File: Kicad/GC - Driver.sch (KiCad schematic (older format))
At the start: 45 parts, among them U3 DRV8302

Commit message: Passives changed from 0805 to 0603
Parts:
- C21, C22, C23, C24, C25, C26, C27, C28, C32, C33, C34, C35, C36, C37: footprint Capacitors_SMD:C_0805 -> Capacitors_SMD:C_0603
- R26, R27, R28, R29, R30, R31, R32, R33, R34, R35, R36, R39, R40, R41, R42, R43: footprint Resistors_SMD:R_0805 -> Resistors_SMD:R_0603
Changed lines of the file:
@@
 F 0 "R36" V 10100 3350 50  0000 C CNN
 F 1 "39k" V 10200 3350 50  0000 C CNN
-F 2 "Resistors_SMD:R_0805" H 10200 3350 60  0001 C CNN
+F 2 "Resistors_SMD:R_0603" H 10200 3350 60  0001 C CNN
 F 3 "" H 10200 3350 60  0001 C CNN
 	1    10200 3350
@@
 F 0 "R39" V 10300 3450 50  0000 C CNN
 F 1 "2k2" V 10200 3450 50  0000 C CNN
-F 2 "Resistors_SMD:R_0805" H 10200 3450 60  0001 C CNN
+F 2 "Resistors_SMD:R_0603" H 10200 3450 60  0001 C CNN
 F 3 "" H 10200 3450 60  0001 C CNN
 	1    10200 3450
@@
 F 0 "R41" V 10300 3950 50  0000 C CNN
 F 1 "2k2" V 10200 3950 50  0000 C CNN
-F 2 "Resistors_SMD:R_0805" H 10200 3950 60  0001 C CNN
+F 2 "Resistors_SMD:R_0603" H 10200 3950 60  0001 C CNN
 F 3 "" H 10200 3950 60  0001 C CNN
 	1    10200 3950
@@
 F 0 "R40" V 10100 3850 50  0000 C CNN
 F 1 "39k" V 10200 3850 50  0000 C CNN
-F 2 "Resistors_SMD:R_0805" H 10200 3850 60  0001 C CNN
+F 2 "Resistors_SMD:R_0603" H 10200 3850 60  0001 C CNN
 F 3 "" H 10200 3850 60  0001 C CNN
 	1    10200 3850
@@
 F 0 "R42" V 10100 4300 50  0000 C CNN
 F 1 "39k" V 10200 4300 50  0000 C CNN
-F 2 "Resistors_SMD:R_0805" H 10200 4300 60  0001 C CNN
+F 2 "Resistors_SMD:R_0603" H 10200 4300 60  0001 C CNN
 F 3 "" H 10200 4300 60  0001 C CNN
 	1    10200 4300
@@
 F 0 "R43" V 10300 4400 50  0000 C CNN
 F 1 "2k2" V 10200 4400 50  0000 C CNN
-F 2 "Resistors_SMD:R_0805" H 10200 4400 60  0001 C CNN
+F 2 "Resistors_SMD:R_0603" H 10200 4400 60  0001 C CNN
 F 3 "" H 10200 4400 60  0001 C CNN
 	1    10200 4400
@@
 F 0 "C34" V 6650 3950 50  0000 L CNN
 F 1 "220nF" V 6550 3950 50  0000 L CNN
-F 2 "Capacitors_SMD:C_0805" H 6600 3850 60  0001 C CNN
+F 2 "Capacitors_SMD:C_0603" H 6600 3850 60  0001 C CNN
 F 3 "" H 6600 3850 60  0001 C CNN
 	1    6600 3850
@@
 F 0 "C35" V 6650 4450 50  0000 L CNN
 F 1 "220nF" V 6550 4450 50  0000 L CNN
-F 2 "Capacitors_SMD:C_0805" H 6600 4350 60  0001 C CNN
+F 2 "Capacitors_SMD:C_0603" H 6600 4350 60  0001 C CNN
 F 3 "" H 6600 4350 60  0001 C CNN
 	1    6600 4350
@@
 F 0 "R31" V 7300 3250 50  0000 C CNN
 F 1 "1M" V 7200 3250 50  0000 C CNN
-F 2 "Resistors_SMD:R_0805" H 7200 3250 60  0001 C CNN
+F 2 "Resistors_SMD:R_0603" H 7200 3250 60  0001 C CNN
 F 3 "" H 7200 3250 60  0001 C CNN
 	1    7200 3250
@@
 F 0 "C27" V 4300 3600 50  0000 L CNN
 F 1 "22nF" V 4300 3950 50  0000 L CNN
-F 2 "Capacitors_SMD:C_0805" H 4350 3850 60  0001 C CNN
+F 2 "Capacitors_SMD:C_0603" H 4350 3850 60  0001 C CNN
 F 3 "" H 4350 3850 60  0001 C CNN
 	1    4350 3850
@@
 F 0 "C22" V 3850 3800 50  0000 L CNN
 F 1 "2.2uF" V 3850 4150 50  0000 L CNN
-F 2 "Capacitors_SMD:C_0805" H 3900 4050 60  0001 C CNN
+F 2 "Capacitors_SMD:C_0603" H 3900 4050 60  0001 C CNN
 F 3 "" H 3900 4050 60  0001 C CNN
 	1    3900 4050
@@
 F 0 "C25" V 4050 4850 50  0000 L CNN
 F 1 "2.2uF" V 3950 4850 50  0000 L CNN
-F 2 "Capacitors_SMD:C_0805" H 4000 4750 60  0001 C CNN
+F 2 "Capacitors_SMD:C_0603" H 4000 4750 60  0001 C CNN
 F 3 "" H 4000 4750 60  0001 C CNN
 	1    4000 4750
@@
 F 0 "R28" V 3850 3150 50  0000 C CNN
 F 1 "10k" V 3950 3150 50  0000 C CNN
-F 2 "Resistors_SMD:R_0805" H 3950 3150 60  0001 C CNN
+F 2 "Resistors_SMD:R_0603" H 3950 3150 60  0001 C CNN
 F 3 "" H 3950 3150 60  0001 C CNN
 	1    3950 3150
@@
 F 0 "R30" V 4600 2300 50  0000 C CNN
 F 1 "220k" V 4500 2300 50  0000 C CNN
-F 2 "Resistors_SMD:R_0805" H 4500 2300 60  0001 C CNN
+F 2 "Resistors_SMD:R_0603" H 4500 2300 60  0001 C CNN
 F 3 "" H 4500 2300 60  0001 C CNN
 	1    4500 2300
@@
 F 0 "C26" H 4050 2200 50  0000 L CNN
 F 1 "6.8nF" H 4250 2200 50  0000 L CNN
-F 2 "Capacitors_SMD:C_0805" H 4250 2100 60  0001 C CNN
+F 2 "Capacitors_SMD:C_0603" H 4250 2100 60  0001 C CNN
 F 3 "" H 4250 2100 60  0001 C CNN
 	1    4250 2100
@@
 F 0 "R32" V 7100 4900 50  0000 C CNN
 F 1 "100R" V 7150 4700 50  0000 C CNN
-F 2 "Resistors_SMD:R_0805" H 7150 4700 60  0001 C CNN
+F 2 "Resistors_SMD:R_0603" H 7150 4700 60  0001 C CNN
 F 3 "" H 7150 4700 60  0001 C CNN
 	1    7150 4700
@@
 F 0 "R34" V 7100 5250 50  0000 C CNN
 F 1 "100R" V 7150 5050 50  0000 C CNN
-F 2 "Resistors_SMD:R_0805" H 7150 5050 60  0001 C CNN
+F 2 "Resistors_SMD:R_0603" H 7150 5050 60  0001 C CNN
 F 3 "" H 7150 5050 60  0001 C CNN
 	1    7150 5050
@@
 F 0 "R35" V 7100 5400 50  0000 C CNN
 F 1 "100R" V 7150 5200 50  0000 C CNN
-F 2 "Resistors_SMD:R_0805" H 7150 5200 60  0001 C CNN
+F 2 "Resistors_SMD:R_0603" H 7150 5200 60  0001 C CNN
 F 3 "" H 7150 5200 60  0001 C CNN
 	1    7150 5200
@@
 F 0 "C36" V 6550 4600 50  0000 L CNN
 F 1 "2.2nF" V 6650 4600 50  0000 L CNN
-F 2 "Capacitors_SMD:C_0805" H 6600 4850 60  0001 C CNN
+F 2 "Capacitors_SMD:C_0603" H 6600 4850 60  0001 C CNN
 F 3 "" H 6600 4850 60  0001 C CNN
 	1    6600 4850
@@
 F 0 "C37" V 6550 4950 50  0000 L CNN
 F 1 "2.2nF" V 6650 4950 50  0000 L CNN
-F 2 "Capacitors_SMD:C_0805" H 6600 5200 60  0001 C CNN
+F 2 "Capacitors_SMD:C_0603" H 6600 5200 60  0001 C CNN
 F 3 "" H 6600 5200 60  0001 C CNN
 	1    6600 5200
@@
 F 0 "C24" V 4050 4600 50  0000 L CNN
 F 1 "2.2uF" V 3950 4600 50  0000 L CNN
-F 2 "Capacitors_SMD:C_0805" H 4000 4500 60  0001 C CNN
+F 2 "Capacitors_SMD:C_0603" H 4000 4500 60  0001 C CNN
 F 3 "" H 4000 4500 60  0001 C CNN
 	1    4000 4500
@@
 F 0 "C21" V 3600 3800 50  0000 L CNN
 F 1 "2.2uF" V 3600 4150 50  0000 L CNN
-F 2 "Capacitors_SMD:C_0805" H 3650 4050 60  0001 C CNN
+F 2 "Capacitors_SMD:C_0603" H 3650 4050 60  0001 C CNN
 F 3 "" H 3650 4050 60  0001 C CNN
 	1    3650 4050
@@
 F 0 "C28" V 4050 5250 50  0000 L CNN
 F 1 "2.2uF" V 3950 5250 50  0000 L CNN
-F 2 "Capacitors_SMD:C_0805" H 4000 5150 60  0001 C CNN
+F 2 "Capacitors_SMD:C_0603" H 4000 5150 60  0001 C CNN
 F 3 "" H 4000 5150 60  0001 C CNN
 	1    4000 5150
@@
 F 0 "R33" V 7100 5050 50  0000 C CNN
 F 1 "100R" V 7150 4850 50  0000 C CNN
-F 2 "Resistors_SMD:R_0805" H 7150 4850 60  0001 C CNN
+F 2 "Resistors_SMD:R_0603" H 7150 4850 60  0001 C CNN
 F 3 "" H 7150 4850 60  0001 C CNN
 	1    7150 4850
@@
 F 0 "C33" V 6650 3450 50  0000 L CNN
 F 1 "220nF" V 6550 3450 50  0000 L CNN
-F 2 "Capacitors_SMD:C_0805" H 6600 3350 60  0001 C CNN
+F 2 "Capacitors_SMD:C_0603" H 6600 3350 60  0001 C CNN
 F 3 "" H 6600 3350 60  0001 C CNN
 	1    6600 3350
@@
 F 0 "C32" V 6650 3050 50  0000 L CNN
 F 1 "100nF" V 6550 3050 50  0000 L CNN
-F 2 "Capacitors_SMD:C_0805" H 6600 2950 60  0001 C CNN
+F 2 "Capacitors_SMD:C_0603" H 6600 2950 60  0001 C CNN
 F 3 "" H 6600 2950 60  0001 C CNN
 	1    6600 2950
@@
 F 0 "R27" V 3550 2950 50  0000 C CNN
 F 1 "3k3" V 3650 2950 50  0000 C CNN
-F 2 "Resistors_SMD:R_0805" H 3650 2950 60  0001 C CNN
+F 2 "Resistors_SMD:R_0603" H 3650 2950 60  0001 C CNN
 F 3 "" H 3650 2950 60  0001 C CNN
 	1    3650 2950
@@
 F 0 "R26" V 3550 2550 50  0000 C CNN
 F 1 "18k" V 3650 2550 50  0000 C CNN
-F 2 "Resistors_SMD:R_0805" H 3650 2550 60  0001 C CNN
+F 2 "Resistors_SMD:R_0603" H 3650 2550 60  0001 C CNN
 F 3 "" H 3650 2550 60  0001 C CNN
 	1    3650 2550
@@
 F 0 "R29" V 4150 2450 50  0000 C CNN
 F 1 "15k" V 4250 2450 50  0000 C CNN
-F 2 "Resistors_SMD:R_0805" H 4250 2450 60  0001 C CNN
+F 2 "Resistors_SMD:R_0603" H 4250 2450 60  0001 C CNN
 F 3 "" H 4250 2450 60  0001 C CNN
 	1    4250 2450
@@
 F 0 "C23" H 3800 2400 50  0000 L CNN
 F 1 "120pF" H 3750 2200 50  0000 L CNN
-F 2 "Capacitors_SMD:C_0805" H 4000 2300 60  0001 C CNN
+F 2 "Capacitors_SMD:C_0603" H 4000 2300 60  0001 C CNN
 F 3 "" H 4000 2300 60  0001 C CNN
 	1    4000 2300

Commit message: Components placed
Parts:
- D4: value 60V 2A -> 60V
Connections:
- net +5V: now also D5.1 (K); no longer D5.2 (A)
- net GND: now also D4.2 (A), D5.2 (A); no longer D4.1 (K), D5.1 (K)
- net at C32.1, L1.1, U3.50 (PH)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: now also D4.1 (K); no longer D4.2 (A)
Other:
- moved on the sheet: C21, C22, C23, C24, C25, C26, C27, C28, C29, C30, C31, C32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

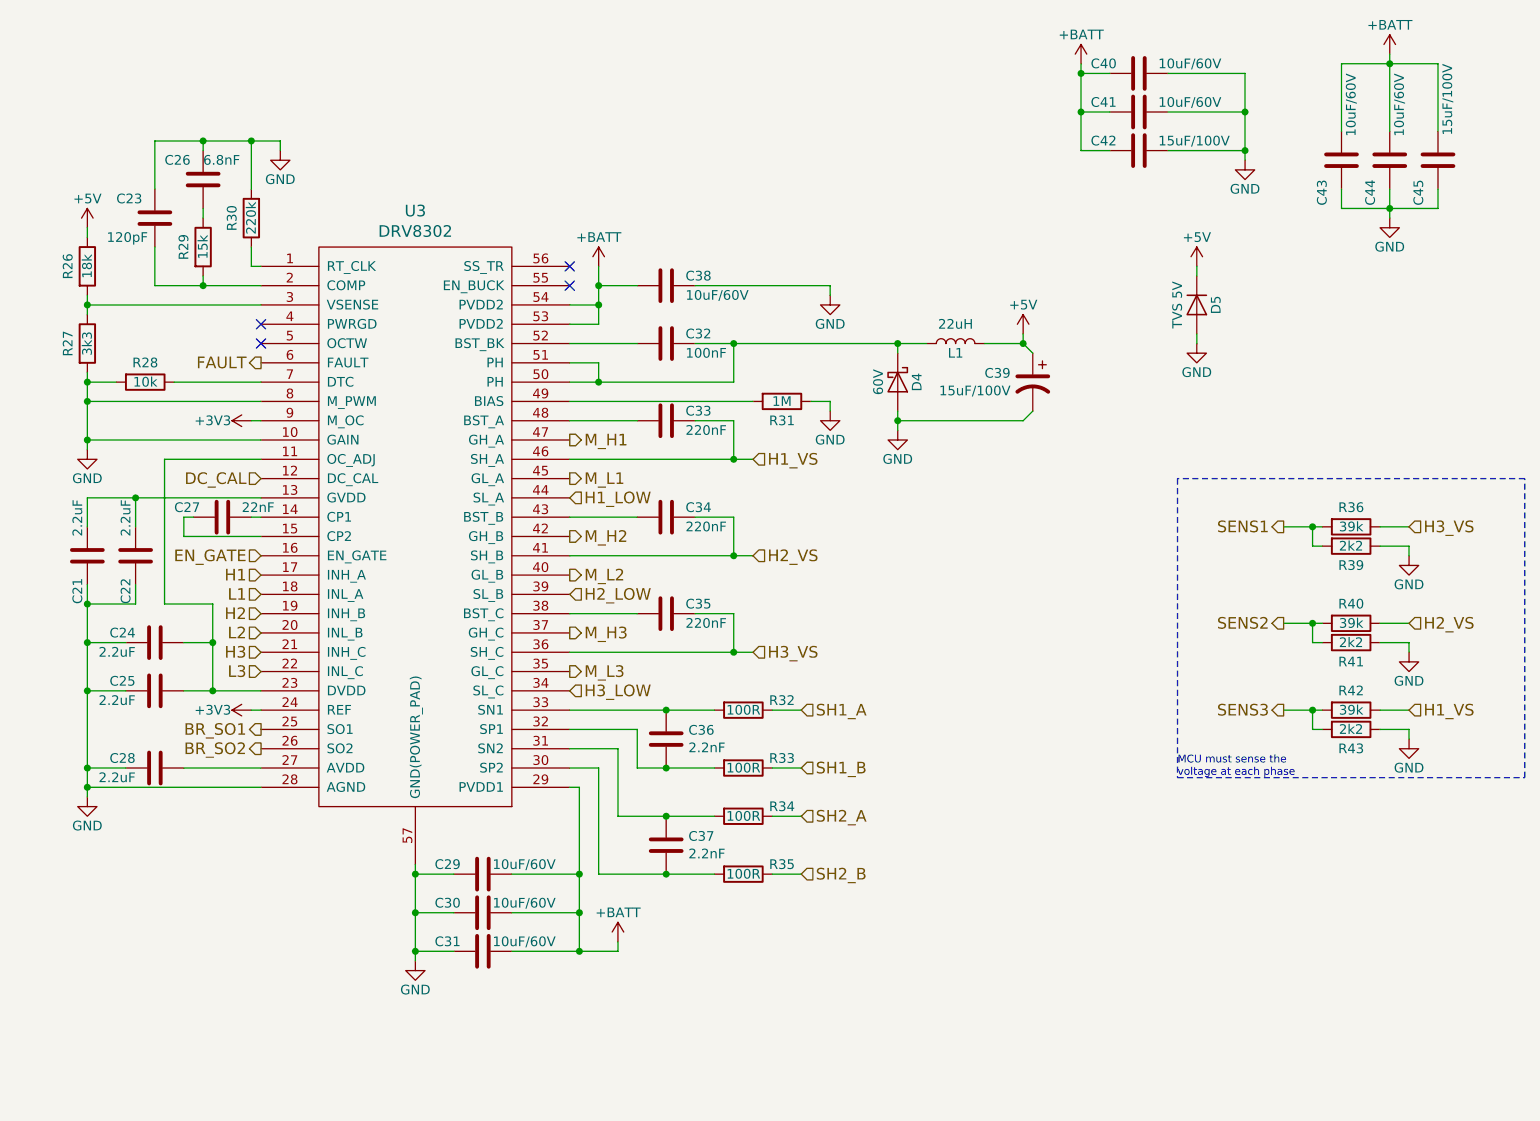
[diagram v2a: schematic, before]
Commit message: Adjusting capacitor size/value
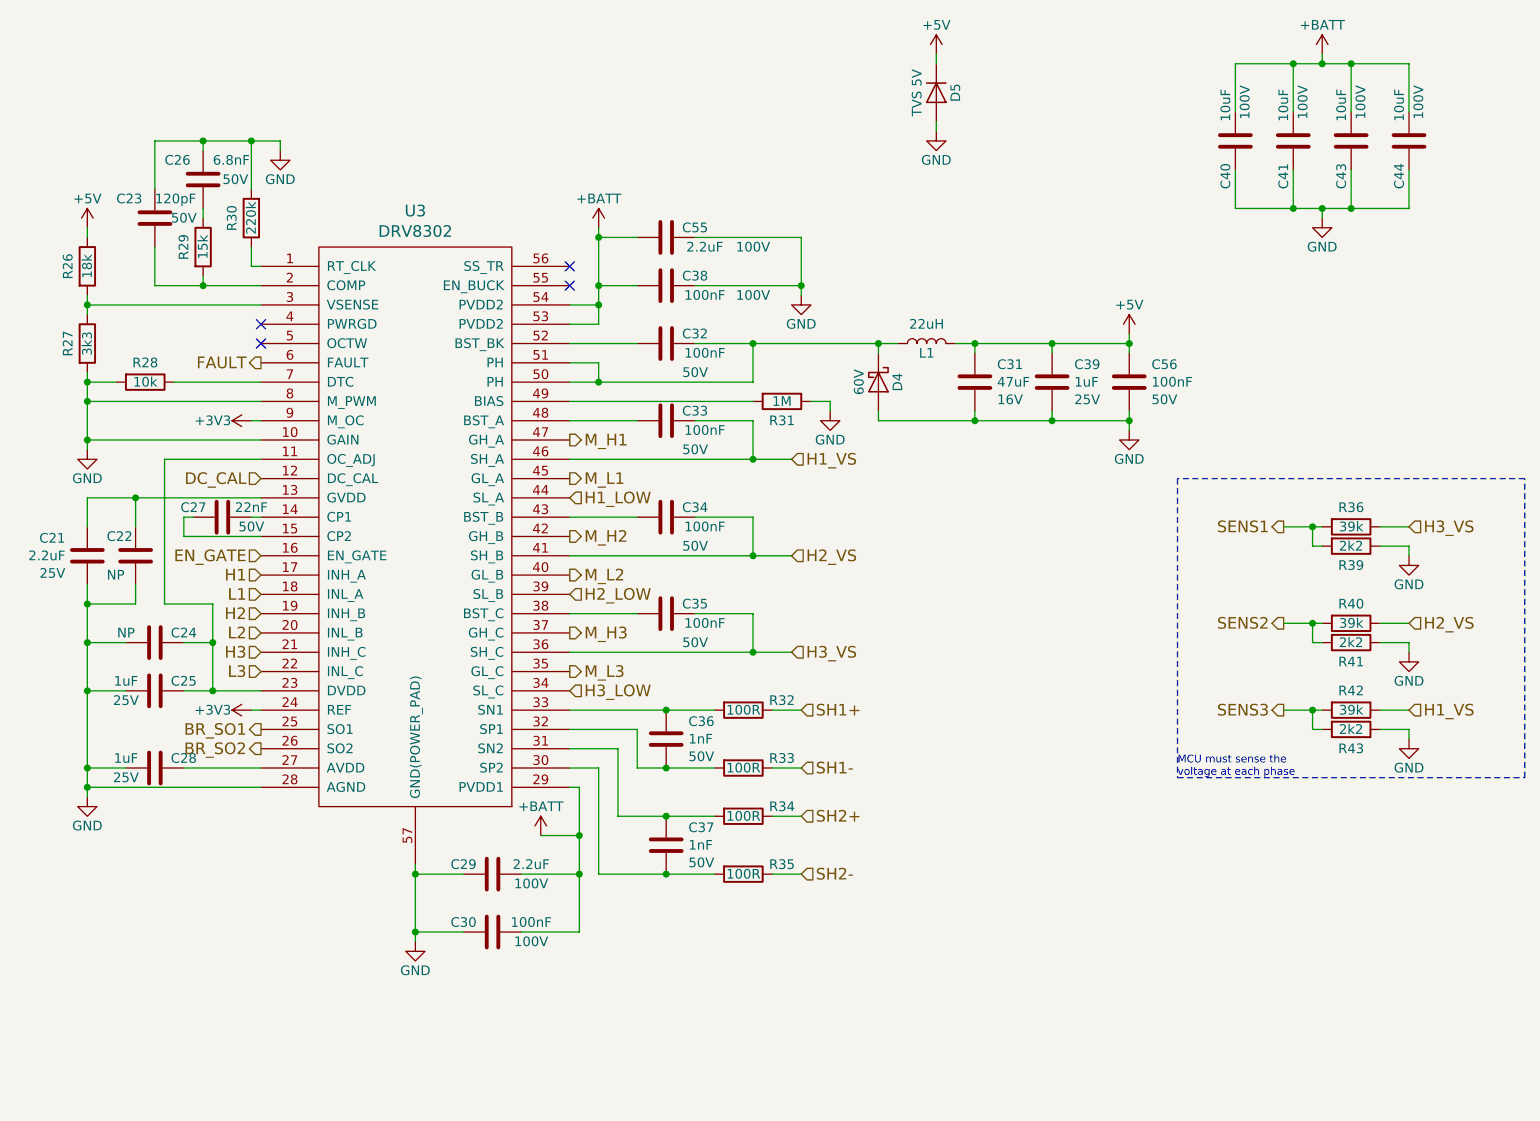
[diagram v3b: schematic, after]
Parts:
- removed C39: 15uF/100V, Capacitors_Tantalum_SMD:CP_Tantalum_Case-B_EIA-3528-21_Reflow, symbol Device:CP1
- removed C42, C45: 15uF/100V, Capacitors_SMD:C_2220, symbol Device:C
- added C39: 1uF, Capacitors_SMD:C_0603, symbol Device:C
- added C55: 2.2uF, Capacitors_SMD:C_1210, symbol Device:C
- added C56: 100nF, Capacitors_SMD:C_0603, symbol Device:C
- C21: Tension (none) -> 25V
- C22, C24: value 2.2uF -> NP; Tension (none) -> (none)
- C23, C26, C27, C32: Tension (none) -> 50V
- C25, C28: value 2.2uF -> 1uF; Tension (none) -> 25V
- C29: value 10uF/60V -> 2.2uF; footprint Capacitors_SMD:C_1206 -> Capacitors_SMD:C_1210; Tension (none) -> 100V
- C30, C38: value 10uF/60V -> 100nF; footprint Capacitors_SMD:C_1206 -> Capacitors_SMD:C_0805; Tension (none) -> 100V
- C31: value 10uF/60V -> 47uF; footprint Capacitors_SMD:C_1206 -> Capacitors_SMD:C_1210; Tension (none) -> 16V
- C33, C34, C35: value 220nF -> 100nF; Tension (none) -> 50V
- C36, C37: value 2.2nF -> 1nF; Tension (none) -> 50V
- C40, C41, C43, C44: value 10uF/60V -> 10uF; Tension (none) -> 100V
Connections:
- net +5V: now also C31.1, C39.1, C56.1
- net +BATT: now also C40.1, C41.1, C43.1, C44.1, C55.2; no longer C31.1, C40.2, C41.2, C43.2, C44.2
- net GND: now also C40.2, C41.2, C43.2, C44.2, C39.2, C55.1, C56.2; no longer C40.1, C41.1, C43.1, C44.1
- net SH1_A renamed SH1+
- net SH1_B renamed SH1-
- net SH2_A renamed SH2+
- net SH2_B renamed SH2-
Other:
- moved on the sheet: C40, C41, D4, D5, L1

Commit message: Fixed libraries issues
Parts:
- C21, C22, C23, C24, C25, C26, C27, C28, C32, C33, C34, C35, C36, C37, C39, C56: footprint Capacitors_SMD:C_0603 -> Capacitor_SMD:C_0603_1608Metric; symbol Device:C -> Gouach_Controller-rescue:C-Device
- C29, C31, C55: footprint Capacitors_SMD:C_1210 -> Capacitor_SMD:C_1210_3225Metric; symbol Device:C -> Gouach_Controller-rescue:C-Device
- C30, C38: footprint Capacitors_SMD:C_0805 -> Capacitor_SMD:C_0805_2012Metric; symbol Device:C -> Gouach_Controller-rescue:C-Device
- C40, C41, C43, C44: footprint Capacitors_SMD:C_1206 -> Capacitor_SMD:C_1206_3216Metric; symbol Device:C -> Gouach_Controller-rescue:C-Device
- D4: footprint Diodes_SMD:D_SOD-123F -> Diode_SMD:D_SOD-123F; symbol Device:D_Schottky -> Gouach_Controller-rescue:D_Schottky-Device
- D5: footprint Diodes_SMD:D_SMA -> Diode_SMD:D_SMA; symbol Device:D -> Gouach_Controller-rescue:D-Device
- L1: footprint Romain:SDR0805 -> Gouach-Controller:SDR0805; symbol Device:L -> Gouach_Controller-rescue:L-Device
- R26, R27, R28, R29, R30, R31, R32, R33, R34, R35, R36, R39, R40, R41, R42, R43: footprint Resistors_SMD:R_0603 -> Resistor_SMD:R_0603_1608Metric; symbol Device:R -> Gouach_Controller-rescue:R-Device
- U3: footprint Romain:DRV8302 -> Gouach-Controller:DRV8302

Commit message: Add Mouser order number
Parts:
- C22, C24: value NP -> (none)
- D4: Mouser (none) -> 771-PMEG6020ER-115; mfg# PMEG6020ER-115 -> (none)
- D5: Mouser (none) -> 652-SMAJ5.0A; mfg# SMAJ5.0A -> (none)
- L1: Mouser (none) -> 652-SDR0805-220ML; mfg# SDR0805 -> (none)
- U3: Mouser (none) -> 595-DRV8302DCA; mfg# DRV8302 -> (none)
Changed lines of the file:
@@
 F 1 "DRV8302" H 5350 4881 60  0000 C CNN
 F 2 "Gouach-Controller:DRV8302" H 5350 3350 60  0001 C CNN
-F 3 "DRV8302" H 5350 3350 60  0001 C CNN
-F 4 "DRV8302" H 5350 3350 50  0001 C CNN "mfg#"
+F 3 "http://www.ti.com/lit/ds/symlink/drv8302.pdf" H 5350 3350 60  0001 C CNN
+F 4 "" H 5350 3350 50  0001 C CNN "mfg#"
+F 5 "595-DRV8302DCA" H 5350 3350 50  0001 C CNN "Mouser"
 	1    5350 3350
 	1    0    0    -1
@@
 F 2 "Gouach-Controller:SDR0805" H 8000 2400 60  0001 C CNN
 F 3 "SDR0805" H 8000 2400 60  0001 C CNN
-F 4 "SDR0805" H 8000 2400 50  0001 C CNN "mfg#"
+F 4 "" H 8000 2400 50  0001 C CNN "mfg#"
+F 5 "652-SDR0805-220ML" H 8000 2400 50  0001 C CNN "Mouser"
 	1    8000 2400
 	0    -1   -1   0
@@
 AR Path="/504F83BE/504FC1DE" Ref="C22"  Part="1"
 F 0 "C22" H 3750 3600 50  0000 L CNN
-F 1 "NP" H 3750 3400 50  0000 L CNN
+F 1 " " H 3750 3400 50  0000 L CNN
 F 2 "Capacitor_SMD:C_0603_1608Metric" H 3900 3500 60  0001 C CNN
 F 3 "" H 3900 3500 60  0001 C CNN
@@
 AR Path="/504F83BE/51094BCE" Ref="C24"  Part="1"
 F 0 "C24" V 4050 3800 50  0000 C CNN
-F 1 "NP" V 4050 4100 50  0000 C CNN
+F 1 " " V 4050 4100 50  0000 C CNN
 F 2 "Capacitor_SMD:C_0603_1608Metric" H 4000 3950 60  0001 C CNN
 F 3 "" H 4000 3950 60  0001 C CNN
@@
 F 1 "TVS 5V" H 8050 1000 50  0000 C CNN
 F 2 "Diode_SMD:D_SMA" H 8050 1100 60  0001 C CNN
-F 3 "SMAJ5.0A" H 8050 1100 60  0001 C CNN
-F 4 "SMAJ5.0A" H 8050 1100 50  0001 C CNN "mfg#"
+F 3 "https://www.vishay.com/docs/88390/smaj50a.pdf" H 8050 1100 60  0001 C CNN
+F 4 "" H 8050 1100 50  0001 C CNN "mfg#"
+F 5 "652-SMAJ5.0A" H 8050 1100 50  0001 C CNN "Mouser"
 	1    8050 1100
 	0    1    1    0
@@
 F 1 "60V" H 7750 2500 50  0000 C CNN
 F 2 "Diode_SMD:D_SOD-123F" H 7750 2600 60  0001 C CNN
-F 3 "PMEG6020ER-115" H 7750 2600 60  0001 C CNN
-F 4 "PMEG6020ER-115" H 7750 2600 50  0001 C CNN "mfg#"
+F 3 "https://assets.nexperia.com/documents/data-sheet/PMEG6020ER.pdf" H 7750 2600 60  0001 C CNN
+F 4 "" H 7750 2600 50  0001 C CNN "mfg#"
+F 5 "771-PMEG6020ER-115" H 7750 2600 50  0001 C CNN "Mouser"
 	1    7750 2600
 	0    1    1    0
